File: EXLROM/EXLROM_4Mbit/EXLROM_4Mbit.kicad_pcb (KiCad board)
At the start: 2 copper layers, 50 x 99 mm, 9 parts, among them J1 EXL100 Cartridge, SW1 SW_DIP_x04, U1 27C040

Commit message: PCB silkscreen update
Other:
- board text added: "EXLROM for the Exelvision EXL100 & Exeltel Brett Hallen, Mar 2025 Port Macquarie, Australia www.youtube.com/@Brfff"
- board text removed: "EXLROM for the Exelvision EXL100 & Exeltel Brett Hallen, Mar 2025 www.youtube.com/@Brfff"
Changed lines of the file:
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@@
 		)
 	)
-	(gr_text "EXLROM for the Exelvision \nEXL100 & Exeltel\nBrett Hallen, Mar 2025\nwww.youtube.com/@Brfff"
+	(gr_text "EXLROM for the Exelvision \nEXL100 & Exeltel\nBrett Hallen, Mar 2025\nPort Macquarie, Australia\nwww.youtube.com/@Brfff"
 		(at 70 52 0)
 		(layer "B.SilkS")

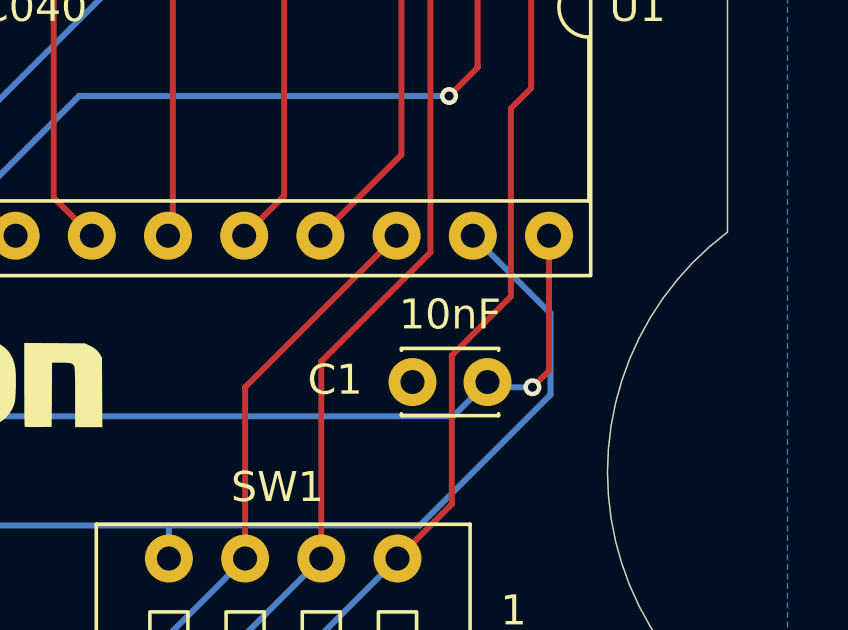
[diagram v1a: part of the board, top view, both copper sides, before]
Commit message: Added ROMs & corrected silkscreen
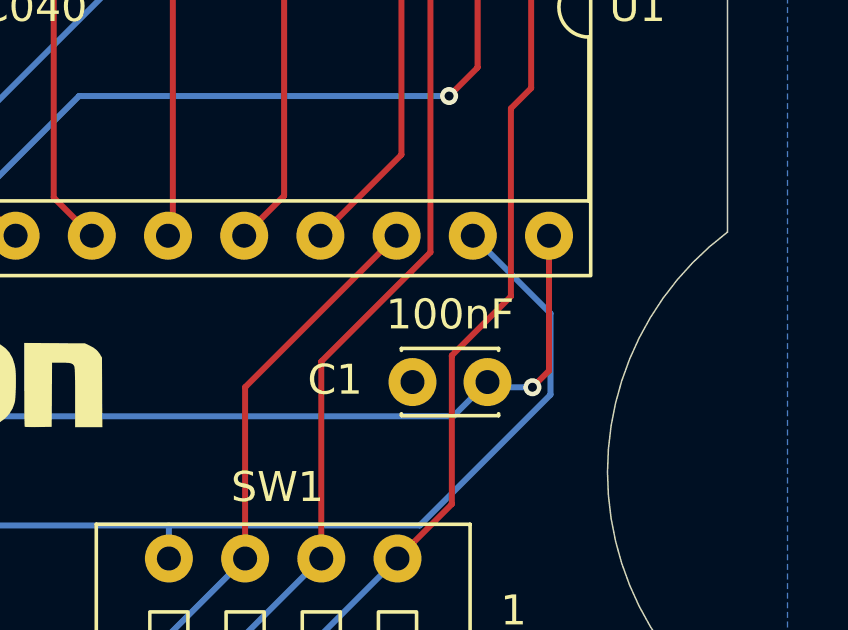
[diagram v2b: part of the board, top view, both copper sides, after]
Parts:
- C1: value 10nF -> 100nF
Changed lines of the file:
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@@
 			)
 		)
-		(property "Value" "10nF"
+		(property "Value" "100nF"
 			(at 1.25 2.25 0)
 			(layer "F.SilkS")
